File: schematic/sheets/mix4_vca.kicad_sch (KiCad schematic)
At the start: 209 parts, among them J1101 WQP518MA, J1102 WQP518MA, J1103 WQP518MA, J1104 WQP518MA, J1105 WQP518MA, J1106 WQP518MA, Q8301 MMBT3906,215, U8301 REF5050AIDR, U8302 ADG5412FBRUZ, U8303 ADG5412FBRUZ, U8304 ADG5412FBRUZ, U8305 ADG5412FBRUZ, U8306 ADG5412FBRUZ, U8307 LM13700M/NOPB, U8308 OPA4197IPWR, U8309 OPA4196IDR, U8310 OPA4196IDR, U8311 OPA4196IDR, U8312 OPA4196IDR, U8313 OPA4196IDR, U8314 OPA4196IDR, U8315 LM393BIDR, U8316 LM393BIDR, U8317 OPA4196IDR, U8318 OPA4196IDR

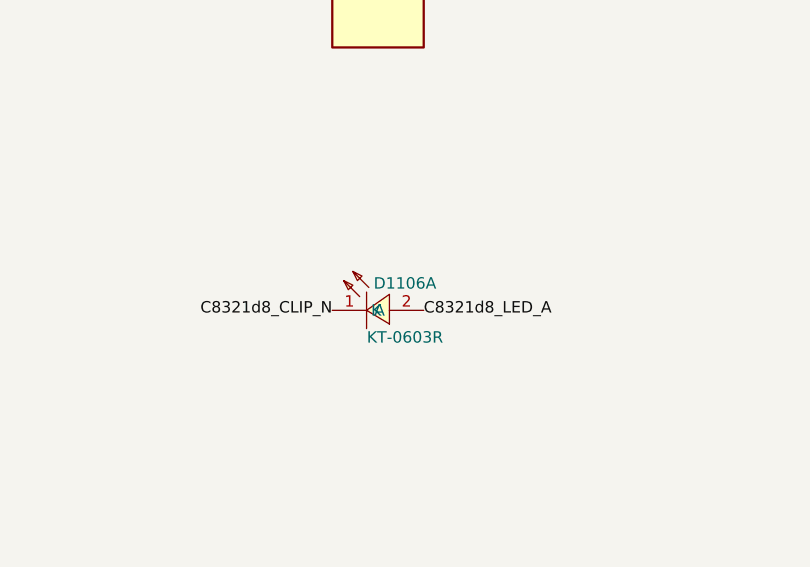
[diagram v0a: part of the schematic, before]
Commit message: Regenerate captured sheets with numeric clip LED references
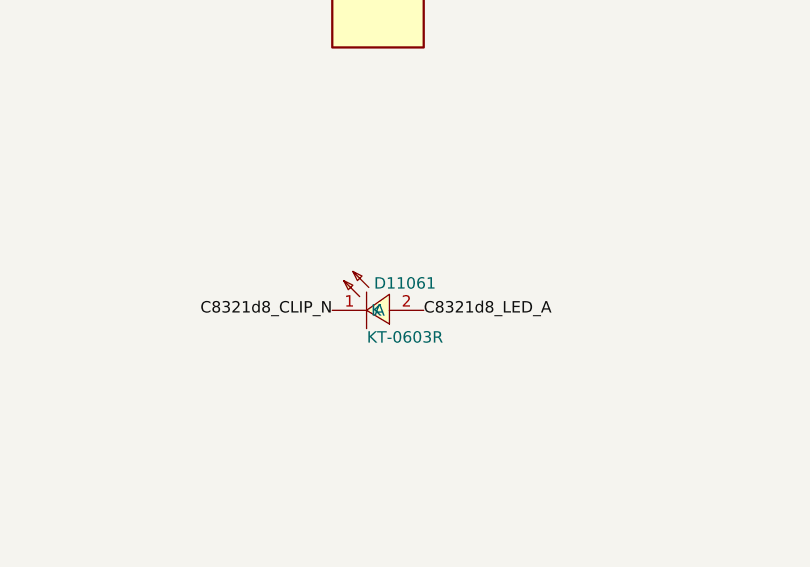
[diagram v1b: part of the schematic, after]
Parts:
- renumbered D1106A to D11061
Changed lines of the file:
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@@
   (symbol (lib_id "zudo-osc-hole-field:KT-0603R") (at 109.22 104.14 0) (unit 0)
     (exclude_from_sim no) (in_bom yes) (on_board yes) (dnp no)
-    (property "Reference" "D1106A" (at 112.22 101.14 0) (effects (font (size 1.27 1.27))))
+    (property "Reference" "D11061" (at 112.22 101.14 0) (effects (font (size 1.27 1.27))))
     (property "Value" "KT-0603R" (at 112.22 107.14 0) (effects (font (size 1.27 1.27))))
     (property "Footprint" "zudo-osc-hole-field:LED0603-RD" (at 109.22 104.14 0) (effects (font (size 1.27 1.27)) (hide yes)))
@@
     (pin "2")
     (instances (project "zudo-osc-hole-field"
-      (path "/bc2f3430-15df-5411-9f37-d35d9a5f2f35/ca0f670c-efb0-5b01-b49f-622dfa3afd0c" (reference "D1106A") (unit 0))
-      (path "/bc2f3430-15df-5411-9f37-d35d9a5f2f35/ec31935f-ceee-5858-ac27-55c8099b53a4" (reference "D1206A") (unit 0))
+      (path "/bc2f3430-15df-5411-9f37-d35d9a5f2f35/ca0f670c-efb0-5b01-b49f-622dfa3afd0c" (reference "D11061") (unit 0))
+      (path "/bc2f3430-15df-5411-9f37-d35d9a5f2f35/ec31935f-ceee-5858-ac27-55c8099b53a4" (reference "D12061") (unit 0))
     ))
   )

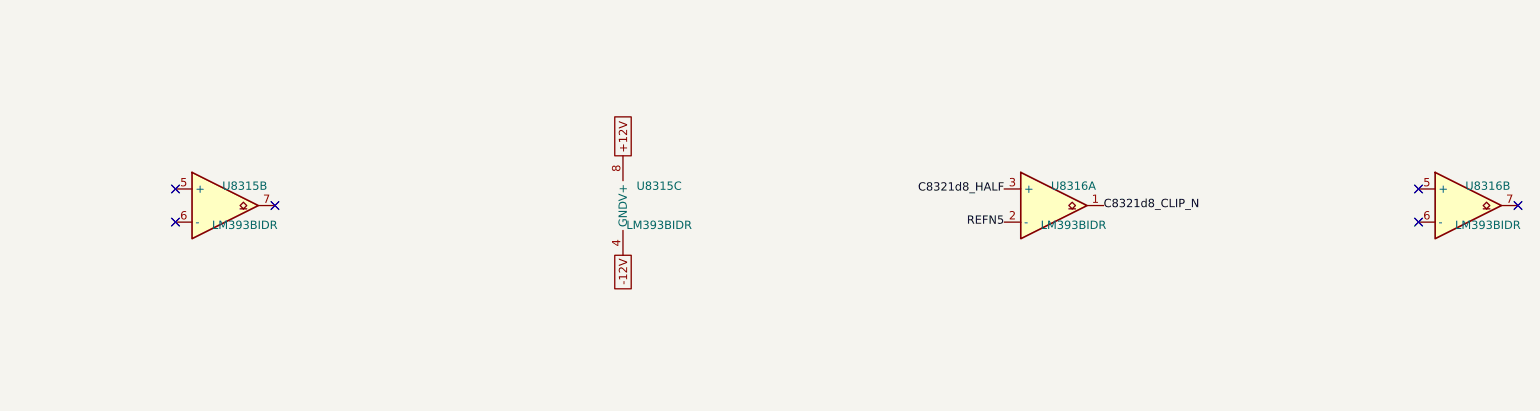
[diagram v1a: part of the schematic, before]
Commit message: Close master schematic integration gates
Audit locked panel coverage, netlist parity, sensitive islands and all active units; terminate spare cells, refresh evidence, and record rail budget overshoot and draft exports.
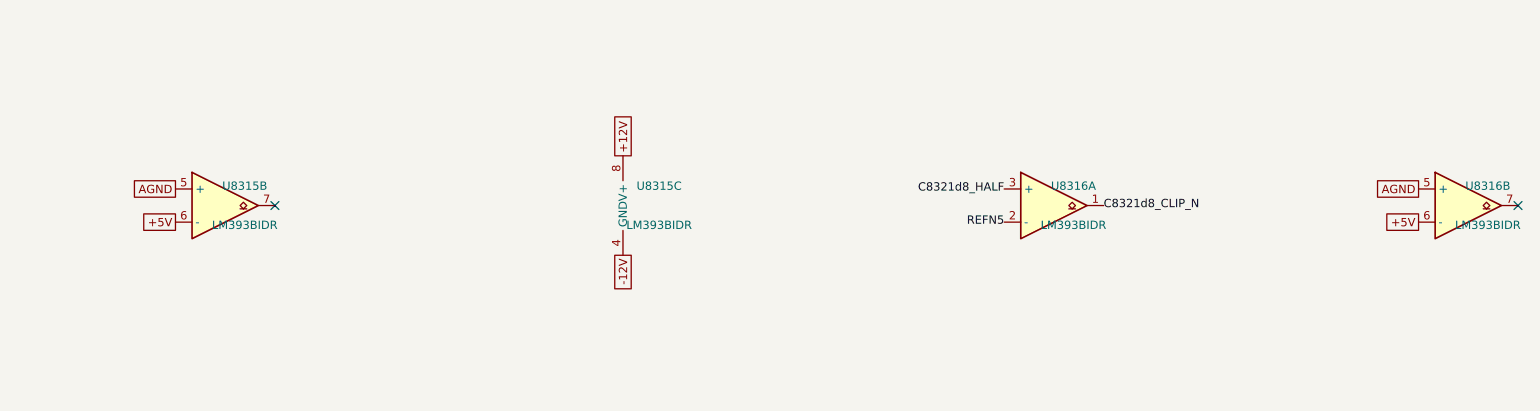
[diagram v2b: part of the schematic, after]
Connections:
- net +5V: now also U8315.6 (-), U8316.6 (-)
- net AGND: now also U8315.5 (+), U8316.5 (+)
- no-connect marks 39 -> 35
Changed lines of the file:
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@@
     ))
   )
-  (no_connect (at 863.6 596.9))
-  (no_connect (at 863.6 601.98))
+  (global_label "AGND" (shape passive) (at 863.6 596.9 0) (effects (font (size 1.27 1.27)) (justify right)))
+  (global_label "+5V" (shape passive) (at 863.6 601.98 0) (effects (font (size 1.27 1.27)) (justify right)))
   (no_connect (at 878.84 599.44))
   (symbol (lib_id "zudo-osc-hole-field:LM393BIDR") (at 934.72 599.44 0) (unit 3)
@@
     ))
   )
-  (no_connect (at 1054.1 596.9))
-  (no_connect (at 1054.1 601.98))
+  (global_label "AGND" (shape passive) (at 1054.1 596.9 0) (effects (font (size 1.27 1.27)) (justify right)))
+  (global_label "+5V" (shape passive) (at 1054.1 601.98 0) (effects (font (size 1.27 1.27)) (justify right)))
   (no_connect (at 1069.34 599.44))
   (symbol (lib_id "zudo-osc-hole-field:LM393BIDR") (at 45.72 637.54 0) (unit 3)

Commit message: Capture non-orderable EXT power boundary
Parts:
- added C8343, C8345: 100 nF, zudo-osc-hole-field:C0603, symbol zudo-osc-hole-field:GRM188R71H104KA93D
- renumbered C8343 to C8344, C8344 to C8346, C8345 to C8347, C8346 to C8348, C8347 to C8349
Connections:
- net -12V: now also C8343.1, C8345.1
- net AGND: now also C8343.2, C8345.2
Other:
- moved on the sheet: C8344, C8346, C8347, C8348, C8349
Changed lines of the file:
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@@
     (property "LCSC" "" (at 871.22 637.54 0) (effects (font (size 1.27 1.27)) (hide yes)))
     (property "Block" "${SHEETNAME}" (at 871.22 637.54 0) (effects (font (size 1.27 1.27)) (hide yes)))
-    (property "Role" "mix4_vca:C_DEC_clip_detector_L_M4A_SUM_clip_SUM__UN_0" (at 871.22 637.54 0) (effects (font (size 1.27 1.27)) (hide yes)))
+    (property "Role" "mix4_vca:C_DEC_clip_detector_L_M4A_SUM_clip_SUM__UP_1" (at 871.22 637.54 0) (effects (font (size 1.27 1.27)) (hide yes)))
     (property "PanelUid" "" (at 871.22 637.54 0) (effects (font (size 1.27 1.27)) (hide yes)))
     (property "Island" "MIX4_VCA_LEDS:${SHEETNAME}" (at 871.22 637.54 0) (effects (font (size 1.27 1.27)) (hide yes)))
@@
     ))
   )
-  (global_label "+12V" (shape passive) (at 866.14 637.54 0) (effects (font (size 1.27 1.27)) (justify right)))
+  (global_label "-12V" (shape passive) (at 866.14 637.54 0) (effects (font (size 1.27 1.27)) (justify right)))
   (global_label "AGND" (shape passive) (at 876.3 637.54 180) (effects (font (size 1.27 1.27)) (justify left)))
   (symbol (lib_id "zudo-osc-hole-field:GRM188R71H104KA93D") (at 934.72 637.54 0) (unit 0)
@@
     (property "LCSC" "" (at 934.72 637.54 0) (effects (font (size 1.27 1.27)) (hide yes)))
     (property "Block" "${SHEETNAME}" (at 934.72 637.54 0) (effects (font (size 1.27 1.27)) (hide yes)))
-    (property "Role" "mix4_vca:C_DEC_PACK_OPA4196IDR_0_0" (at 934.72 637.54 0) (effects (font (size 1.27 1.27)) (hide yes)))
+    (property "Role" "mix4_vca:C_DEC_clip_detector_L_M4A_SUM_clip_SUM__UN_0" (at 934.72 637.54 0) (effects (font (size 1.27 1.27)) (hide yes)))
     (property "PanelUid" "" (at 934.72 637.54 0) (effects (font (size 1.27 1.27)) (hide yes)))
     (property "Island" "MIX4_VCA_LEDS:${SHEETNAME}" (at 934.72 637.54 0) (effects (font (size 1.27 1.27)) (hide yes)))
@@
     (property "LCSC" "" (at 998.22 637.54 0) (effects (font (size 1.27 1.27)) (hide yes)))
     (property "Block" "${SHEETNAME}" (at 998.22 637.54 0) (effects (font (size 1.27 1.27)) (hide yes)))
-    (property "Role" "mix4_vca:C_DEC_PACK_OPA4196IDR_0_1" (at 998.22 637.54 0) (effects (font (size 1.27 1.27)) (hide yes)))
+    (property "Role" "mix4_vca:C_DEC_clip_detector_L_M4A_SUM_clip_SUM__UN_1" (at 998.22 637.54 0) (effects (font (size 1.27 1.27)) (hide yes)))
     (property "PanelUid" "" (at 998.22 637.54 0) (effects (font (size 1.27 1.27)) (hide yes)))
     (property "Island" "MIX4_VCA_LEDS:${SHEETNAME}" (at 998.22 637.54 0) (effects (font (size 1.27 1.27)) (hide yes)))
@@
     (property "LCSC" "" (at 1061.72 637.54 0) (effects (font (size 1.27 1.27)) (hide yes)))
     (property "Block" "${SHEETNAME}" (at 1061.72 637.54 0) (effects (font (size 1.27 1.27)) (hide yes)))
-    (property "Role" "mix4_vca:C_DEC_PACK_OPA4196IDR_1_0" (at 1061.72 637.54 0) (effects (font (size 1.27 1.27)) (hide yes)))
+    (property "Role" "mix4_vca:C_DEC_PACK_OPA4196IDR_0_0" (at 1061.72 637.54 0) (effects (font (size 1.27 1.27)) (hide yes)))
     (property "PanelUid" "" (at 1061.72 637.54 0) (effects (font (size 1.27 1.27)) (hide yes)))
     (property "Island" "MIX4_VCA_LEDS:${SHEETNAME}" (at 1061.72 637.54 0) (effects (font (size 1.27 1.27)) (hide yes)))
@@
     (property "LCSC" "" (at 45.72 675.64 0) (effects (font (size 1.27 1.27)) (hide yes)))
     (property "Block" "${SHEETNAME}" (at 45.72 675.64 0) (effects (font (size 1.27 1.27)) (hide yes)))
-    (property "Role" "mix4_vca:C_DEC_PACK_OPA4196IDR_1_1" (at 45.72 675.64 0) (effects (font (size 1.27 1.27)) (hide yes)))
+    (property "Role" "mix4_vca:C_DEC_PACK_OPA4196IDR_0_1" (at 45.72 675.64 0) (effects (font (size 1.27 1.27)) (hide yes)))
     (property "PanelUid" "" (at 45.72 675.64 0) (effects (font (size 1.27 1.27)) (hide yes)))
     (property "Island" "MIX4_VCA_LEDS:${SHEETNAME}" (at 45.72 675.64 0) (effects (font (size 1.27 1.27)) (hide yes)))
@@
   (global_label "-12V" (shape passive) (at 40.64 675.64 0) (effects (font (size 1.27 1.27)) (justify right)))
   (global_label "AGND" (shape passive) (at 50.8 675.64 180) (effects (font (size 1.27 1.27)) (justify left)))
+  (symbol (lib_id "zudo-osc-hole-field:GRM188R71H104KA93D") (at 109.22 675.64 0) (unit 0)
+    (exclude_from_sim no) (in_bom yes) (on_board yes) (dnp no)
+    (property "Reference" "C8348" (at 112.22 672.64 0) (effects (font (size 1.27 1.27))))
+    (property "Value" "100 nF" (at 112.22 678.64 0) (effects (font (size 1.27 1.27))))
+    (property "Footprint" "zudo-osc-hole-field:C0603" (at 109.22 675.64 0) (effects (font (size 1.27 1.27)) (hide yes)))
+    (property "Datasheet" "" (at 109.22 675.64 0) (effects (font (size 1.27 1.27)) (hide yes)))
+    (property "MPN" "GRM188R71H104KA93D" (at 109.22 675.64 0) (effects (font (size 1.27 1.27)) (hide yes)))
+    (property "Manufacturer" "Murata" (at 109.22 675.64 0) (effects (font (size 1.27 1.27)) (hide yes)))
+    (property "LCSC" "" (at 109.22 675.64 0) (effects (font (size 1.27 1.27)) (hide yes)))
+    (property "Block" "${SHEETNAME}" (at 109.22 675.64 0) (effects (font (size 1.27 1.27)) (hide yes)))
+    (property "Role" "mix4_vca:C_DEC_PACK_OPA4196IDR_1_0" (at 109.22 675.64 0) (effects (font (size 1.27 1.27)) (hide yes)))
+    (property "PanelUid" "" (at 109.22 675.64 0) (effects (font (size 1.27 1.27)) (hide yes)))
+    (property "Island" "MIX4_VCA_LEDS:${SHEETNAME}" (at 109.22 675.64 0) (effects (font (size 1.27 1.27)) (hide yes)))
+    (property "Sensitive" "" (at 109.22 675.64 0) (effects (font (size 1.27 1.27)) (hide yes)))
+    (pin "1")
+    (pin "2")
+    (instances (project "zudo-osc-hole-field"
+      (path "/bc2f3430-15df-5411-9f37-d35d9a5f2f35/ca0f670c-efb0-5b01-b49f-622dfa3afd0c" (reference "C8348") (unit 0))
+      (path "/bc2f3430-15df-5411-9f37-d35d9a5f2f35/ec31935f-ceee-5858-ac27-55c8099b53a4" (reference "C8448") (unit 0))
+    ))
+  )
+  (global_label "+12V" (shape passive) (at 104.14 675.64 0) (effects (font (size 1.27 1.27)) (justify right)))
+  (global_label "AGND" (shape passive) (at 114.3 675.64 180) (effects (font (size 1.27 1.27)) (justify left)))
+  (symbol (lib_id "zudo-osc-hole-field:GRM188R71H104KA93D") (at 172.72 675.64 0) (unit 0)
+    (exclude_from_sim no) (in_bom yes) (on_board yes) (dnp no)
+    (property "Reference" "C8349" (at 175.72 672.64 0) (effects (font (size 1.27 1.27))))
+    (property "Value" "100 nF" (at 175.72 678.64 0) (effects (font (size 1.27 1.27))))
+    (property "Footprint" "zudo-osc-hole-field:C0603" (at 172.72 675.64 0) (effects (font (size 1.27 1.27)) (hide yes)))
+    (property "Datasheet" "" (at 172.72 675.64 0) (effects (font (size 1.27 1.27)) (hide yes)))
+    (property "MPN" "GRM188R71H104KA93D" (at 172.72 675.64 0) (effects (font (size 1.27 1.27)) (hide yes)))
+    (property "Manufacturer" "Murata" (at 172.72 675.64 0) (effects (font (size 1.27 1.27)) (hide yes)))
+    (property "LCSC" "" (at 172.72 675.64 0) (effects (font (size 1.27 1.27)) (hide yes)))
+    (property "Block" "${SHEETNAME}" (at 172.72 675.64 0) (effects (font (size 1.27 1.27)) (hide yes)))
+    (property "Role" "mix4_vca:C_DEC_PACK_OPA4196IDR_1_1" (at 172.72 675.64 0) (effects (font (size 1.27 1.27)) (hide yes)))
+    (property "PanelUid" "" (at 172.72 675.64 0) (effects (font (size 1.27 1.27)) (hide yes)))
+    (property "Island" "MIX4_VCA_LEDS:${SHEETNAME}" (at 172.72 675.64 0) (effects (font (size 1.27 1.27)) (hide yes)))
+    (property "Sensitive" "" (at 172.72 675.64 0) (effects (font (size 1.27 1.27)) (hide yes)))
+    (pin "1")
+    (pin "2")
+    (instances (project "zudo-osc-hole-field"
+      (path "/bc2f3430-15df-5411-9f37-d35d9a5f2f35/ca0f670c-efb0-5b01-b49f-622dfa3afd0c" (reference "C8349") (unit 0))
+      (path "/bc2f3430-15df-5411-9f37-d35d9a5f2f35/ec31935f-ceee-5858-ac27-55c8099b53a4" (reference "C8449") (unit 0))
+    ))
+  )
+  (global_label "-12V" (shape passive) (at 167.64 675.64 0) (effects (font (size 1.27 1.27)) (justify right)))
+  (global_label "AGND" (shape passive) (at 177.8 675.64 180) (effects (font (size 1.27 1.27)) (justify left)))
   (embedded_fonts no)
 )

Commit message: Refine source I/O regions and preserve whole package boundaries
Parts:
- added C8350, C8351: 100 nF, zudo-osc-hole-field:C0603, symbol zudo-osc-hole-field:GRM188R71H104KA93D
- added U8319: OPA4196IDR, zudo-osc-hole-field:SOIC-14_3.9x8.7mm_P1.27mm, symbol zudo-osc-hole-field:OPA4196IDR
- C8301, C8302, C8303, C8304, C8305, C8306, C8307, C8308, C8309, C8310, C8311, C8312, C8313, C8314, D8313, D8314, Q8301, R8301, R8302, R8303, R8304, R8309, R8310, R8311, R8312, R8313, R8314, R8319, R8320, R8321, R8322, R8323, R8324, R8329, R8330, R8331, R8332, R8333, R8334, R8339, R8340, R8341, R8342, R8343, R8344, R8345, R8346, R8347, R8348, R8349, R8354, R8355, R8356, R8357, R8358, R8359, R8360, R8361, R8362, R8363, R8364, R8365, R8366, R8367, R8368, R8369, R8370, R8371, R8372, R8373, R8374, R8375, R8376, R8377, R8378, R8379, R8380, RV8307, RV8308, U8301, U8307, U8308: BoardRegion (none) -> core
- C8315: BoardRegion (none) -> core; Decouples (none) -> G1_reference_generator_J_M4A_1_LOCAL__U
- C8316, C8317: BoardRegion (none) -> jack; Decouples (none) -> G1_input_fault_switch_J_M4A_1_1__U; Island MIX4_VCA_CORE:${SHEETNAME} -> IO_JACK:${SHEETNAME}
- C8318, C8319: BoardRegion (none) -> jack; Decouples (none) -> G1_input_fault_switch_J_M4A_1_2__U; Island MIX4_VCA_CORE:${SHEETNAME} -> IO_JACK:${SHEETNAME}
- C8320, C8321: BoardRegion (none) -> jack; Decouples (none) -> G1_input_fault_switch_J_M4A_1_3__U; Island MIX4_VCA_CORE:${SHEETNAME} -> IO_JACK:${SHEETNAME}
- C8322, C8323: BoardRegion (none) -> jack; Decouples (none) -> G1_input_fault_switch_J_M4A_1_4__U; Island MIX4_VCA_CORE:${SHEETNAME} -> IO_JACK:${SHEETNAME}
- C8324, C8325: BoardRegion (none) -> jack; Decouples (none) -> G1_input_fault_switch_J_M4A_1_ATTEN__U; Island MIX4_VCA_CORE:${SHEETNAME} -> IO_JACK:${SHEETNAME}
- C8326, C8327: BoardRegion (none) -> core; Decouples (none) -> G1_VCA_OTA
- C8328, C8329: BoardRegion (none) -> jack; Decouples (none) -> G2_clip_detector_L_M4A_SUM_clip_SUM__UP; Island MIX4_VCA_CORE:${SHEETNAME} -> IO_JACK:${SHEETNAME}
- C8330, C8331: BoardRegion (none) -> jack; Decouples (none) -> G2_clip_detector_L_M4A_SUM_clip_SUM__UN; Island MIX4_VCA_CORE:${SHEETNAME} -> IO_JACK:${SHEETNAME}
- C8332, C8333: BoardRegion (none) -> core; Decouples (none) -> G1_PACK_OPA4197IPWR_0; Island MIX4_VCA_CORE:${SHEETNAME} -> IO_CORE:${SHEETNAME}
- C8334, C8335: BoardRegion (none) -> core; Decouples (none) -> G1_PACK_OPA4196IDR_0; Island MIX4_VCA_CORE:${SHEETNAME} -> IO_CORE:${SHEETNAME}
- C8336, C8337: BoardRegion (none) -> core; Decouples (none) -> G1_PACK_OPA4196IDR_1; Island MIX4_VCA_CORE:${SHEETNAME} -> IO_CORE:${SHEETNAME}
- C8338, C8339: BoardRegion (none) -> core; Decouples (none) -> G1_PACK_OPA4196IDR_2; Island MIX4_VCA_CORE:${SHEETNAME} -> IO_CORE:${SHEETNAME}
- C8340, C8341: BoardRegion (none) -> core; Decouples (none) -> G1_PACK_OPA4196IDR_3; Island MIX4_VCA_CORE:${SHEETNAME} -> IO_CORE:${SHEETNAME}
- C8342, C8343: BoardRegion (none) -> core; Decouples (none) -> G1_PACK_OPA4196IDR_4; Island MIX4_VCA_LEDS:${SHEETNAME} -> IO_CORE:${SHEETNAME}
- C8344, C8345: BoardRegion (none) -> jack; Decouples (none) -> G1_PACK_OPA4196IDR_5; Island MIX4_VCA_LEDS:${SHEETNAME} -> IO_JACK:${SHEETNAME}
- C8346, C8347: BoardRegion (none) -> jack; Decouples (none) -> G2_PACK_OPA4196IDR_0; Island MIX4_VCA_LEDS:${SHEETNAME} -> IO_JACK:${SHEETNAME}
- C8348, C8349: BoardRegion (none) -> jack; Decouples (none) -> G2_PACK_OPA4196IDR_1; Island MIX4_VCA_LEDS:${SHEETNAME} -> IO_JACK:${SHEETNAME}
- D1101, D1102, D1103, D1104, D1105, D1106, D11061, J1101, J1102, J1103, J1104, J1105, J1106: BoardRegion (none) -> jack; Island (none) -> IO_JACK:${SHEETNAME}
- D8308, D8309, D8310, D8311, D8312, R8305, R8306, R8307, R8308, R8315, R8316, R8317, R8318, R8325, R8326, R8327, R8328, R8335, R8336, R8337, R8338, R8350, R8351, R8352, R8353, R8381, R8382, U8302, U8303, U8304, U8305, U8306, U8314: BoardRegion (none) -> jack; Island MIX4_VCA_CORE:${SHEETNAME} -> IO_JACK:${SHEETNAME}
- D8315, D8316, D8317, D8318, D8319, D8320, D8321, D8322, D8323, D8324, D8325, D8326, D8327, D8328, D8329, D8330, D8331, D8332, D8333, D8334, D8335, D8336, D8337, D8338, R8383, R8384, R8385, R8386, R8387, R8388, R8389, R8390, R8391, U8315, U8316, U8317, U8318: BoardRegion (none) -> jack; Island MIX4_VCA_LEDS:${SHEETNAME} -> IO_JACK:${SHEETNAME}
- RV1101, RV1102, RV1103, RV1104, RV1105, RV1106: BoardRegion (none) -> control; Island (none) -> IO_CONTROL:${SHEETNAME}
- U8308, U8309, U8310, U8311, U8312, U8313: BoardRegion (none) -> core; Island MIX4_VCA_CORE:${SHEETNAME} -> IO_CORE:${SHEETNAME}
- U8309: BoardRegion (none) -> core; LogicalCellKey high_impedance_input_J_M4A_1_2__A.1 -> bipolar_attenuverter_C_M4A_2__2__A.1; Role high_impedance_input:A -> bipolar_attenuverter:A
- U8309: BoardRegion (none) -> core; LogicalCellKey bipolar_attenuverter_C_M4A_1__1__A.1 -> remote_buffer_J_M4A_1_2__A.1; Role bipolar_attenuverter:A -> remote_buffer:A
- U8309: BoardRegion (none) -> core; LogicalCellKey remote_buffer_J_M4A_1_1__A.1 -> bipolar_attenuverter_C_M4A_1__1__A.1; Role remote_buffer:A -> bipolar_attenuverter:A
- U8309: BoardRegion (none) -> core; LogicalCellKey high_impedance_input_J_M4A_1_1__A.1 -> remote_buffer_J_M4A_1_1__A.1; Role high_impedance_input:A -> remote_buffer:A
- U8310: BoardRegion (none) -> core; LogicalCellKey remote_buffer_J_M4A_1_3__A.1 -> bipolar_attenuverter_C_M4A_4__4__A.1; Role remote_buffer:A -> bipolar_attenuverter:A
- U8310: BoardRegion (none) -> core; LogicalCellKey high_impedance_input_J_M4A_1_3__A.1 -> remote_buffer_J_M4A_1_4__A.1; Role high_impedance_input:A -> remote_buffer:A
- U8310: BoardRegion (none) -> core; LogicalCellKey bipolar_attenuverter_C_M4A_2__2__A.1 -> bipolar_attenuverter_C_M4A_3__3__A.1
- U8310: BoardRegion (none) -> core; LogicalCellKey remote_buffer_J_M4A_1_2__A.1 -> remote_buffer_J_M4A_1_3__A.1
- U8311: BoardRegion (none) -> core; LogicalCellKey remote_buffer_J_M4A_1_4__A.1 -> bipolar_attenuverter_C_M4A_CV__CV__A.1; Role remote_buffer:A -> bipolar_attenuverter:A
- U8311: BoardRegion (none) -> core; LogicalCellKey bipolar_attenuverter_C_M4A_4__4__A.1 -> dc_control_source_C_M4A_LEVEL_LEVEL__A.1; Role bipolar_attenuverter:A -> dc_control_source:A
- U8311: BoardRegion (none) -> core; LogicalCellKey high_impedance_input_J_M4A_1_4__A.1 -> remote_buffer_J_M4A_1_ATTEN__A.1; Role high_impedance_input:A -> remote_buffer:A
- U8311: BoardRegion (none) -> core; LogicalCellKey bipolar_attenuverter_C_M4A_3__3__A.1 -> SUMMER.1; Role bipolar_attenuverter:A -> mix4_vca:SUMMER; Sensitive (none) -> SUM_NODE
- U8312: BoardRegion (none) -> core; LogicalCellKey SUMMER.1 -> COMMAND_SUM.1; Role mix4_vca:SUMMER -> mix4_vca:COMMAND_SUM; Sensitive SUM_NODE -> (none)
- U8312: BoardRegion (none) -> core; LogicalCellKey remote_buffer_J_M4A_1_ATTEN__A.1 -> COMMAND_BUFFER.1; Role remote_buffer:A -> mix4_vca:COMMAND_BUFFER
- U8312: BoardRegion (none) -> core; LogicalCellKey high_impedance_input_J_M4A_1_ATTEN__A.1 -> COMMAND_INVERT.1; Role high_impedance_input:A -> mix4_vca:COMMAND_INVERT
- U8312: BoardRegion (none) -> core; LogicalCellKey bipolar_attenuverter_C_M4A_CV__CV__A.1 -> EMITTER_TARGET.1; Role bipolar_attenuverter:A -> mix4_vca:EMITTER_TARGET
- U8313: BoardRegion (none) -> core; Island MIX4_VCA_CORE:${SHEETNAME} -> IO_CORE:${SHEETNAME}; LogicalCellKey COMMAND_BUFFER.1 -> (none); Role mix4_vca:COMMAND_BUFFER -> mix4_vca:unused grounded follower
- U8313: BoardRegion (none) -> core; Island MIX4_VCA_CORE:${SHEETNAME} -> IO_CORE:${SHEETNAME}; LogicalCellKey COMMAND_INVERT.1 -> (none); Role mix4_vca:COMMAND_INVERT -> mix4_vca:unused grounded follower
- U8313: BoardRegion (none) -> core; LogicalCellKey dc_control_source_C_M4A_LEVEL_LEVEL__A.1 -> CURRENT_SERVO.1; Role dc_control_source:A -> mix4_vca:CURRENT_SERVO; Sensitive (none) -> EMITTER
- U8313: BoardRegion (none) -> core; LogicalCellKey COMMAND_SUM.1 -> CURRENT_TO_VOLTAGE.1; Role mix4_vca:COMMAND_SUM -> mix4_vca:CURRENT_TO_VOLTAGE; Sensitive (none) -> OTA_CURRENT
- U8314: BoardRegion (none) -> jack; Island MIX4_VCA_CORE:${SHEETNAME} -> IO_JACK:${SHEETNAME}; LogicalCellKey CURRENT_SERVO.1 -> high_impedance_input_J_M4A_1_2__A.1; Role mix4_vca:CURRENT_SERVO -> high_impedance_input:A; Sensitive EMITTER -> (none)
- U8314: BoardRegion (none) -> jack; Island MIX4_VCA_CORE:${SHEETNAME} -> IO_JACK:${SHEETNAME}; LogicalCellKey general_output_J_M4A_1_SUM__A.1 -> high_impedance_input_J_M4A_1_4__A.1; Role general_output:A -> high_impedance_input:A
- U8314: BoardRegion (none) -> jack; Island MIX4_VCA_CORE:${SHEETNAME} -> IO_JACK:${SHEETNAME}; LogicalCellKey CURRENT_TO_VOLTAGE.1 -> high_impedance_input_J_M4A_1_3__A.1; Role mix4_vca:CURRENT_TO_VOLTAGE -> high_impedance_input:A; Sensitive OTA_CURRENT -> (none)
- U8314: BoardRegion (none) -> jack; Island MIX4_VCA_CORE:${SHEETNAME} -> IO_JACK:${SHEETNAME}; LogicalCellKey EMITTER_TARGET.1 -> high_impedance_input_J_M4A_1_1__A.1; Role mix4_vca:EMITTER_TARGET -> high_impedance_input:A
- U8317: BoardRegion (none) -> jack; Island MIX4_VCA_LEDS:${SHEETNAME} -> IO_JACK:${SHEETNAME}; LogicalCellKey magnitude_indicator_L_M4A_3_mag_3__A.1 -> magnitude_indicator_L_M4A_1_mag_1__A.1
- U8317: BoardRegion (none) -> jack; Island MIX4_VCA_LEDS:${SHEETNAME} -> IO_JACK:${SHEETNAME}; LogicalCellKey magnitude_indicator_L_M4A_2_mag_2__A.1 -> general_output_J_M4A_1_SUM__A.1; Role magnitude_indicator:A -> general_output:A
- U8317: BoardRegion (none) -> jack; Island MIX4_VCA_LEDS:${SHEETNAME} -> IO_JACK:${SHEETNAME}; LogicalCellKey magnitude_indicator_L_M4A_4_mag_4__A.1 -> magnitude_indicator_L_M4A_2_mag_2__A.1
- U8317: BoardRegion (none) -> jack; Island MIX4_VCA_LEDS:${SHEETNAME} -> IO_JACK:${SHEETNAME}; LogicalCellKey magnitude_indicator_L_M4A_1_mag_1__A.1 -> high_impedance_input_J_M4A_1_ATTEN__A.1; Role magnitude_indicator:A -> high_impedance_input:A
- U8318: BoardRegion (none) -> jack; Island MIX4_VCA_LEDS:${SHEETNAME} -> IO_JACK:${SHEETNAME}; LogicalCellKey (none) -> magnitude_indicator_L_M4A_SUM_mag_SUM__A.1; Role mix4_vca:unused grounded follower -> magnitude_indicator:A
- U8318: BoardRegion (none) -> jack; Island MIX4_VCA_LEDS:${SHEETNAME} -> IO_JACK:${SHEETNAME}; LogicalCellKey clip_detector_L_M4A_SUM_clip_SUM__A.1 -> magnitude_indicator_L_M4A_ATTEN_mag_ATTEN__A.1; Role clip_detector:A -> magnitude_indicator:A
- U8318: BoardRegion (none) -> jack; Island MIX4_VCA_LEDS:${SHEETNAME} -> IO_JACK:${SHEETNAME}; LogicalCellKey magnitude_indicator_L_M4A_ATTEN_mag_ATTEN__A.1 -> magnitude_indicator_L_M4A_3_mag_3__A.1
- U8318: BoardRegion (none) -> jack; Island MIX4_VCA_LEDS:${SHEETNAME} -> IO_JACK:${SHEETNAME}; LogicalCellKey magnitude_indicator_L_M4A_SUM_mag_SUM__A.1 -> magnitude_indicator_L_M4A_4_mag_4__A.1
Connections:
- net +12V: now also C8350.1, U8319.4 (V+)
- net -12V: now also C8351.1, U8319.11 (V-)
- net 1_BUFFER: now also U8309.3 (+), U8314.1, U8314.2 (-); no longer U8309.1, U8309.2 (-), U8309.5 (+)
- net 1_GAIN: now also U8309.7, U8317.10 (+); no longer U8309.8, U8317.3 (+)
- net 2_BUFFER: now also U8309.10 (+), U8314.6 (-), U8314.7; no longer U8309.13 (-), U8309.14, U8310.3 (+)
- net 2_GAIN: now also U8309.14, U8317.12 (+); no longer U8310.7, U8317.5 (+)
- net 3_BUFFER: now also U8310.3 (+), U8314.8, U8314.9 (-); no longer U8310.12 (+), U8310.8, U8310.9 (-)
- net 3_GAIN: now also U8310.7, U8318.3 (+); no longer U8311.1, U8317.10 (+)
- net 4_BUFFER: now also U8310.10 (+), U8314.13 (-), U8314.14; no longer U8311.10 (+), U8311.6 (-), U8311.7
- net 4_GAIN: now also U8310.14, U8318.5 (+); no longer U8311.14, U8317.12 (+)
- net AGND: now also U8311.3 (+), U8312.5 (+), U8313.12 (+), C8350.2, C8351.2, U8319.10 (+), U8319.12 (+), U8319.5 (+); no longer U8314.10 (+), U8318.12 (+)
- net ATTEN_BUFFER: now also U8311.5 (+), U8317.1, U8317.2 (-), U8318.10 (+); no longer U8312.10 (+), U8312.6 (-), U8312.7, U8318.3 (+)
- net BASE_DRIVE: now also U8313.1; no longer U8314.7
- net C154038_SUM: now also U8310.13 (-); no longer U8311.13 (-)
- net C154038_W_SENSE: now also U8310.12 (+); no longer U8311.12 (+)
- net C1c45d6_W_SENSE: now also U8311.12 (+); no longer U8313.3 (+)
- net C2006b9_DRIVE: now also U8310.1; no longer U8310.14
- net C2006b9_FB: now also U8310.2 (-); no longer U8310.13 (-)
- net C2169e5_DRIVE: now also U8318.1; no longer U8317.8
- net C2169e5_SENSE: now also U8318.2 (-); no longer U8317.9 (-)
- net C24ce01_SUM: now also U8311.9 (-); no longer U8312.13 (-)
- net C24ce01_W_SENSE: now also U8311.10 (+); no longer U8312.12 (+)
- net C2be340_SENSE: now also U8314.12 (+); no longer U8311.5 (+)
- net C320656_DRIVE: now also U8318.8; no longer U8318.1
- net C320656_SENSE: now also U8318.9 (-); no longer U8318.2 (-)
- net C38051c_SUM: now also U8310.6 (-); no longer U8311.2 (-)
- net C38051c_W_SENSE: now also U8310.5 (+); no longer U8311.3 (+)
- net C412fd1_DRIVE: now also U8317.8; no longer U8317.1
- net C412fd1_SENSE: now also U8317.9 (-); no longer U8317.2 (-)
- net C5eb398_SENSE: now also U8314.5 (+); no longer U8309.12 (+)
- net C75c2e7_SUM: now also U8309.6 (-); no longer U8309.9 (-)
- net C75c2e7_W_SENSE: now also U8309.5 (+); no longer U8309.10 (+)
- net C7750d4_SENSE: now also U8314.10 (+); no longer U8310.10 (+)
- net C797803_DRIVE: now also U8309.1; no longer U8309.7
- net C797803_FB: now also U8309.2 (-); no longer U8309.6 (-)
- net C8321d8_BUF: now also U8319.1, U8319.2 (-); no longer U8318.8, U8318.9 (-)
- net C865f36_DRIVE: now also U8310.8; no longer U8311.8
- net C865f36_FB: now also U8310.9 (-); no longer U8311.9 (-)
- net C93bba0_DRIVE: now also U8317.14; no longer U8317.7
- net C93bba0_SENSE: now also U8317.13 (-); no longer U8317.6 (-)
- net COMMAND: now also U8312.8, U8312.9 (-); no longer U8313.13 (-), U8313.14
- net COMMAND_CLAMP: now also U8312.10 (+); no longer U8313.12 (+)
- net COMMAND_INVERT_SUM: now also U8312.6 (-); no longer U8313.9 (-)
- net COMMAND_NEG: now also U8312.1; no longer U8313.7
- net COMMAND_RAW: now also U8312.7; no longer U8313.8
- net COMMAND_SUM: now also U8312.2 (-); no longer U8313.6 (-)
- net CV_DEPTH: now also U8311.8; no longer U8312.14
- net Ca1191c_SUM: now also U8309.13 (-); no longer U8310.6 (-)
- net Ca1191c_W_SENSE: now also U8309.12 (+); no longer U8310.5 (+)
- net Caeced9_SENSE: now also U8314.3 (+); no longer U8309.3 (+)
- net Cb5ae41_SENSE: now also U8317.3 (+); no longer U8312.5 (+)
- net Ccb7527_DRIVE: now also U8311.7; no longer U8312.8
- net Ccb7527_FB: now also U8311.6 (-); no longer U8312.9 (-)
- net Cd59875_DRIVE: now also U8318.14; no longer U8318.7
- net Cd59875_SENSE: now also U8318.13 (-); no longer U8318.6 (-)
- net Cea264a_DRIVE: now also U8317.6 (-), U8317.7; no longer U8314.13 (-), U8314.14
- net Cf876de_DRIVE: now also U8318.7; no longer U8317.14
- net Cf876de_SENSE: now also U8318.6 (-); no longer U8317.13 (-)
- net Cfaa69a_DRIVE: now also U8309.8; no longer U8310.1
- net Cfaa69a_FB: now also U8309.9 (-); no longer U8310.2 (-)
- net EMITTER: now also U8313.2 (-); no longer U8314.6 (-)
- net EMITTER_TARGET: now also U8312.14, U8313.3 (+); no longer U8314.1, U8314.5 (+)
- net LEVEL_MANUAL: now also U8311.13 (-), U8311.14; no longer U8313.1, U8313.2 (-)
- net OTA_CURRENT: now also U8313.6 (-); no longer U8314.9 (-)
- net REF25: now also U8312.12 (+); no longer U8314.3 (+)
- net SUM_NODE: now also U8311.2 (-); no longer U8312.2 (-)
- net SUM_POSTVCA: now also U8313.7, U8317.5 (+), U8318.12 (+); no longer U8314.12 (+), U8314.8, U8318.5 (+)
- net SUM_PRELEVEL: now also U8311.1, U8319.3 (+); no longer U8312.1, U8318.10 (+)
- net TARGET_SUM: now also U8312.13 (-); no longer U8314.2 (-)
- removed net PACK_OPA4196IDR_1_UNUSED3: U8318.13 (-), U8318.14
- net PACK_OPA4197IPWR_0_UNUSED3 renamed G1_PACK_OPA4197IPWR_0_IO_UNUSED4
- new net G1_PACK_OPA4196IDR_4_IO_UNUSED3: U8313.8, U8313.9 (-)
- new net G1_PACK_OPA4196IDR_4_IO_UNUSED4: U8313.13 (-), U8313.14
- new net IO_EXTRA_19_IO_UNUSED2: U8319.6 (-), U8319.7
- new net IO_EXTRA_19_IO_UNUSED3: U8319.8, U8319.9 (-)
- new net IO_EXTRA_19_IO_UNUSED4: U8319.13 (-), U8319.14
